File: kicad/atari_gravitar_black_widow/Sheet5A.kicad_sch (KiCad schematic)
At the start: 121 parts, among them Q2 2N6044, Q3 2N6044, Q4 2N6044

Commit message: more caps
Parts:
- C30, C33, C34: footprint Star_Wars_Vector_PCB:GenericComp -> Star_Wars_Vector_PCB:CapYellow
- C31, C32: footprint Star_Wars_Vector_PCB:SmallCap -> Star_Wars_Vector_PCB:CapBrown
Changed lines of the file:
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@@
       (effects (font (size 1.27 1.27)) (justify left))
     )
-    (property "Footprint" "Star_Wars_Vector_PCB:GenericComp" (id 2) (at 429.26 173.6598 0)
+    (property "Footprint" "Star_Wars_Vector_PCB:CapYellow" (id 2) (at 429.26 173.6598 0)
       (effects (font (size 1.27 1.27)) hide)
     )
@@
       (effects (font (size 1.27 1.27)) (justify left))
     )
-    (property "Footprint" "Star_Wars_Vector_PCB:GenericComp" (id 2) (at 445.135 111.4298 0)
+    (property "Footprint" "Star_Wars_Vector_PCB:CapYellow" (id 2) (at 445.135 111.4298 0)
       (effects (font (size 1.27 1.27)) hide)
     )
@@
       (effects (font (size 1.27 1.27)) (justify left))
     )
-    (property "Footprint" "Star_Wars_Vector_PCB:GenericComp" (id 2) (at 417.83 151.4348 0)
+    (property "Footprint" "Star_Wars_Vector_PCB:CapYellow" (id 2) (at 417.83 151.4348 0)
       (effects (font (size 1.27 1.27)) hide)
     )
@@
       (effects (font (size 1.27 1.27)) (justify left))
     )
-    (property "Footprint" "Star_Wars_Vector_PCB:SmallCap" (id 2) (at 385.7498 109.855 0)
+    (property "Footprint" "Star_Wars_Vector_PCB:CapBrown" (id 2) (at 385.7498 109.855 0)
       (effects (font (size 1.27 1.27)) hide)
     )
@@
       (effects (font (size 1.27 1.27)) (justify left))
     )
-    (property "Footprint" "Star_Wars_Vector_PCB:SmallCap" (id 2) (at 385.7498 172.085 0)
-      (effects (font (size 1.27 1.27)) hide)
-    )
+    (property "Footprint" "Star_Wars_Vector_PCB:CapBrown" (id 2) (at 385.7498 172.085 0)
+      (effects (font (size 1.27 1.27)) hide)
+    )

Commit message: more cap placements
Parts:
- C100, C101, C103, C104, C105, C106, C107, C108, C114, C115, C116, C90, C91, C92, C93, C94, C95, C96, C97, C98, C99: footprint (none) -> Star_Wars_Vector_PCB:GenericComp
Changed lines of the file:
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@@
       (effects (font (size 1.27 1.27)) (justify left))
     )
-    (property "Footprint" "" (id 2) (at 167.9702 234.95 0)
+    (property "Footprint" "Star_Wars_Vector_PCB:GenericComp" (id 2) (at 167.9702 234.95 0)
       (effects (font (size 1.27 1.27)) hide)
     )
@@
       (effects (font (size 1.27 1.27)) (justify left))
     )
-    (property "Footprint" "" (id 2) (at 133.6802 128.27 0)
+    (property "Footprint" "Star_Wars_Vector_PCB:GenericComp" (id 2) (at 133.6802 128.27 0)
       (effects (font (size 1.27 1.27)) hide)
     )
@@
       (effects (font (size 1.27 1.27)) (justify left))
     )
-    (property "Footprint" "" (id 2) (at 140.6652 128.27 0)
+    (property "Footprint" "Star_Wars_Vector_PCB:GenericComp" (id 2) (at 140.6652 128.27 0)
       (effects (font (size 1.27 1.27)) hide)
     )
@@
       (effects (font (size 1.27 1.27)) (justify left))
     )
-    (property "Footprint" "" (id 2) (at 126.6952 304.8 0)
+    (property "Footprint" "Star_Wars_Vector_PCB:GenericComp" (id 2) (at 126.6952 304.8 0)
       (effects (font (size 1.27 1.27)) hide)
     )
@@
       (effects (font (size 1.27 1.27)) (justify left))
     )
-    (property "Footprint" "" (id 2) (at 119.7102 304.8 0)
+    (property "Footprint" "Star_Wars_Vector_PCB:GenericComp" (id 2) (at 119.7102 304.8 0)
       (effects (font (size 1.27 1.27)) hide)
     )
@@
       (effects (font (size 1.27 1.27)) (justify left))
     )
-    (property "Footprint" "" (id 2) (at 154.6352 234.95 0)
+    (property "Footprint" "Star_Wars_Vector_PCB:GenericComp" (id 2) (at 154.6352 234.95 0)
       (effects (font (size 1.27 1.27)) hide)
     )
@@
       (effects (font (size 1.27 1.27)) (justify left))
     )
-    (property "Footprint" "" (id 2) (at 119.7102 128.27 0)
+    (property "Footprint" "Star_Wars_Vector_PCB:GenericComp" (id 2) (at 119.7102 128.27 0)
       (effects (font (size 1.27 1.27)) hide)
     )
@@
       (effects (font (size 1.27 1.27)) (justify left))
     )
-    (property "Footprint" "" (id 2) (at 160.9852 128.27 0)
+    (property "Footprint" "Star_Wars_Vector_PCB:GenericComp" (id 2) (at 160.9852 128.27 0)
       (effects (font (size 1.27 1.27)) hide)
     )
@@
       (effects (font (size 1.27 1.27)) (justify left))
     )
-    (property "Footprint" "" (id 2) (at 112.7252 304.8 0)
+    (property "Footprint" "Star_Wars_Vector_PCB:GenericComp" (id 2) (at 112.7252 304.8 0)
       (effects (font (size 1.27 1.27)) hide)
     )
@@
       (effects (font (size 1.27 1.27)) (justify left))
     )
-    (property "Footprint" "" (id 2) (at 154.0002 128.27 0)
+    (property "Footprint" "Star_Wars_Vector_PCB:GenericComp" (id 2) (at 154.0002 128.27 0)
       (effects (font (size 1.27 1.27)) hide)
     )
@@
       (effects (font (size 1.27 1.27)) (justify left))
     )
-    (property "Footprint" "" (id 2) (at 378.1552 294.64 0)
+    (property "Footprint" "Star_Wars_Vector_PCB:GenericComp" (id 2) (at 378.1552 294.64 0)
       (effects (font (size 1.27 1.27)) hide)
     )
@@
       (effects (font (size 1.27 1.27)) (justify left))
     )
-    (property "Footprint" "" (id 2) (at 140.6652 234.95 0)
+    (property "Footprint" "Star_Wars_Vector_PCB:GenericComp" (id 2) (at 140.6652 234.95 0)
       (effects (font (size 1.27 1.27)) hide)
     )
@@
       (effects (font (size 1.27 1.27)) (justify left))
     )
-    (property "Footprint" "" (id 2) (at 126.6952 128.27 0)
+    (property "Footprint" "Star_Wars_Vector_PCB:GenericComp" (id 2) (at 126.6952 128.27 0)
       (effects (font (size 1.27 1.27)) hide)
     )
@@
       (effects (font (size 1.27 1.27)) (justify left))
     )
-    (property "Footprint" "" (id 2) (at 167.9702 128.27 0)
+    (property "Footprint" "Star_Wars_Vector_PCB:GenericComp" (id 2) (at 167.9702 128.27 0)
       (effects (font (size 1.27 1.27)) hide)
     )
@@
       (effects (font (size 1.27 1.27)) (justify left))
     )
-    (property "Footprint" "" (id 2) (at 147.0152 128.27 0)
+    (property "Footprint" "Star_Wars_Vector_PCB:GenericComp" (id 2) (at 147.0152 128.27 0)
       (effects (font (size 1.27 1.27)) hide)
     )
@@
       (effects (font (size 1.27 1.27)) (justify left))
     )
-    (property "Footprint" "" (id 2) (at 147.6502 234.95 0)
+    (property "Footprint" "Star_Wars_Vector_PCB:GenericComp" (id 2) (at 147.6502 234.95 0)
       (effects (font (size 1.27 1.27)) hide)
     )
@@
       (effects (font (size 1.27 1.27)) (justify left))
     )
-    (property "Footprint" "" (id 2) (at 378.1552 271.78 0)
+    (property "Footprint" "Star_Wars_Vector_PCB:GenericComp" (id 2) (at 378.1552 271.78 0)
       (effects (font (size 1.27 1.27)) hide)
     )
@@
       (effects (font (size 1.27 1.27)) (justify left))
     )
-    (property "Footprint" "" (id 2) (at 378.1552 313.055 0)
+    (property "Footprint" "Star_Wars_Vector_PCB:GenericComp" (id 2) (at 378.1552 313.055 0)
       (effects (font (size 1.27 1.27)) hide)
     )
@@
       (effects (font (size 1.27 1.27)) (justify left))
     )
-    (property "Footprint" "" (id 2) (at 161.6202 234.95 0)
+    (property "Footprint" "Star_Wars_Vector_PCB:GenericComp" (id 2) (at 161.6202 234.95 0)
       (effects (font (size 1.27 1.27)) hide)
     )
@@
       (effects (font (size 1.27 1.27)) (justify left))
     )
-    (property "Footprint" "" (id 2) (at 105.7402 304.8 0)
+    (property "Footprint" "Star_Wars_Vector_PCB:GenericComp" (id 2) (at 105.7402 304.8 0)
       (effects (font (size 1.27 1.27)) hide)
     )
@@
       (effects (font (size 1.27 1.27)) (justify left))
     )
-    (property "Footprint" "" (id 2) (at 133.0452 304.8 0)
-      (effects (font (size 1.27 1.27)) hide)
-    )
+    (property "Footprint" "Star_Wars_Vector_PCB:GenericComp" (id 2) (at 133.0452 304.8 0)
+      (effects (font (size 1.27 1.27)) hide)
+    )

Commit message: more cap placements
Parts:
- C31, C32: footprint Star_Wars_Vector_PCB:CapBrown -> quantum_arcade_pcb:CapSmall
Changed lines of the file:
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@@
       (effects (font (size 1.27 1.27)) (justify left))
     )
-    (property "Footprint" "Star_Wars_Vector_PCB:CapBrown" (id 2) (at 385.7498 109.855 0)
+    (property "Footprint" "quantum_arcade_pcb:CapSmall" (id 2) (at 385.7498 109.855 0)
       (effects (font (size 1.27 1.27)) hide)
     )
@@
       (effects (font (size 1.27 1.27)) (justify left))
     )
-    (property "Footprint" "Star_Wars_Vector_PCB:CapBrown" (id 2) (at 385.7498 172.085 0)
+    (property "Footprint" "quantum_arcade_pcb:CapSmall" (id 2) (at 385.7498 172.085 0)
       (effects (font (size 1.27 1.27)) hide)
     )

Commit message: resistor placements R1-R153
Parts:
- C30: footprint Star_Wars_Vector_PCB:CapYellow -> Star_Wars_Vector_PCB:CapElec2
- R102, R103, R104, R105, R106, R108, R109, R110, R111, R112, R113, R114, R115, R116, R117, R118, R119, R121, R122, R123, R124, R125, R126, R127, R128, R129, R130, R131, R133, R134, R135, R136, R137, R138, R139, R140, R141, R142, R143, R144, R145, R146, R147, R148, R24, R25, R26, R27, R28, R29, R30, R31, R32, R33, R34, R35, R36, R37, R38, R39, R43, R44, R45, R46, R47, R48, R49, R50, R51, R52, R53, R54: footprint (none) -> Star_Wars_Vector_PCB:GenericComp

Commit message: caps
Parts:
- C30: footprint Star_Wars_Vector_PCB:CapElec2 -> Star_Wars_Vector_PCB:Inductor1
- C33: footprint Star_Wars_Vector_PCB:CapYellow -> Star_Wars_Vector_PCB:Inductor1
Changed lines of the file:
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@@
       (effects (font (size 1.27 1.27)) (justify left))
     )
-    (property "Footprint" "Star_Wars_Vector_PCB:CapYellow" (id 2) (at 429.26 173.6598 0)
+    (property "Footprint" "Star_Wars_Vector_PCB:Inductor1" (id 2) (at 429.26 173.6598 0)
       (effects (font (size 1.27 1.27)) hide)
     )
@@
       (effects (font (size 1.27 1.27)) (justify left))
     )
-    (property "Footprint" "Star_Wars_Vector_PCB:CapElec2" (id 2) (at 445.135 111.4298 0)
+    (property "Footprint" "Star_Wars_Vector_PCB:Inductor1" (id 2) (at 445.135 111.4298 0)
       (effects (font (size 1.27 1.27)) hide)
     )

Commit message: ALL PARTS PLACED!!
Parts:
- B_4, D_4: footprint (none) -> Star_Wars_Vector_PCB:DIP16
- P_10: footprint (none) -> Star_Wars_Vector_PCB:DIP8
- Q2, Q3, Q4: footprint (none) -> quantum_arcade_pcb:BigTrans
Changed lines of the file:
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@@
     (property "Reference" "B_4" (id 0) (at 287.02 89.9668 0))
     (property "Value" "8 DIP SW" (id 1) (at 287.02 87.6554 0))
-    (property "Footprint" "" (id 2) (at 287.02 75.565 0)
+    (property "Footprint" "Star_Wars_Vector_PCB:DIP16" (id 2) (at 287.02 75.565 0)
       (effects (font (size 1.27 1.27)) hide)
     )
@@
       (effects (font (size 1.27 1.27)) (justify left))
     )
-    (property "Footprint" "" (id 2) (at 361.95 306.705 0)
+    (property "Footprint" "quantum_arcade_pcb:BigTrans" (id 2) (at 361.95 306.705 0)
       (effects (font (size 1.27 1.27)) hide)
     )
@@
     (property "Reference" "P_10" (id 0) (at 395.605 316.0735 0))
     (property "Value" "SW4POS" (id 1) (at 395.605 318.8486 0))
-    (property "Footprint" "" (id 2) (at 395.605 325.12 0)
+    (property "Footprint" "Star_Wars_Vector_PCB:DIP8" (id 2) (at 395.605 325.12 0)
       (effects (font (size 1.27 1.27)) hide)
     )
@@
       (effects (font (size 1.27 1.27)) (justify left))
     )
-    (property "Footprint" "" (id 2) (at 361.95 265.43 0)
+    (property "Footprint" "quantum_arcade_pcb:BigTrans" (id 2) (at 361.95 265.43 0)
       (effects (font (size 1.27 1.27)) hide)
     )
@@
     (property "Reference" "D_4" (id 0) (at 287.02 152.1968 0))
     (property "Value" "8 DIP SW" (id 1) (at 287.02 149.8854 0))
-    (property "Footprint" "" (id 2) (at 287.02 137.795 0)
+    (property "Footprint" "Star_Wars_Vector_PCB:DIP16" (id 2) (at 287.02 137.795 0)
       (effects (font (size 1.27 1.27)) hide)
     )
@@
       (effects (font (size 1.27 1.27)) (justify left))
     )
-    (property "Footprint" "" (id 2) (at 361.95 288.29 0)
+    (property "Footprint" "quantum_arcade_pcb:BigTrans" (id 2) (at 361.95 288.29 0)
       (effects (font (size 1.27 1.27)) hide)
     )
@@
     (property "Reference" "P_10" (id 0) (at 86.36 181.4535 0))
     (property "Value" "SW4POS" (id 1) (at 86.36 184.2286 0))
-    (property "Footprint" "" (id 2) (at 86.36 190.5 0)
-      (effects (font (size 1.27 1.27)) hide)
-    )
+    (property "Footprint" "Star_Wars_Vector_PCB:DIP8" (id 2) (at 86.36 190.5 0)
+      (effects (font (size 1.27 1.27)) hide)
+    )

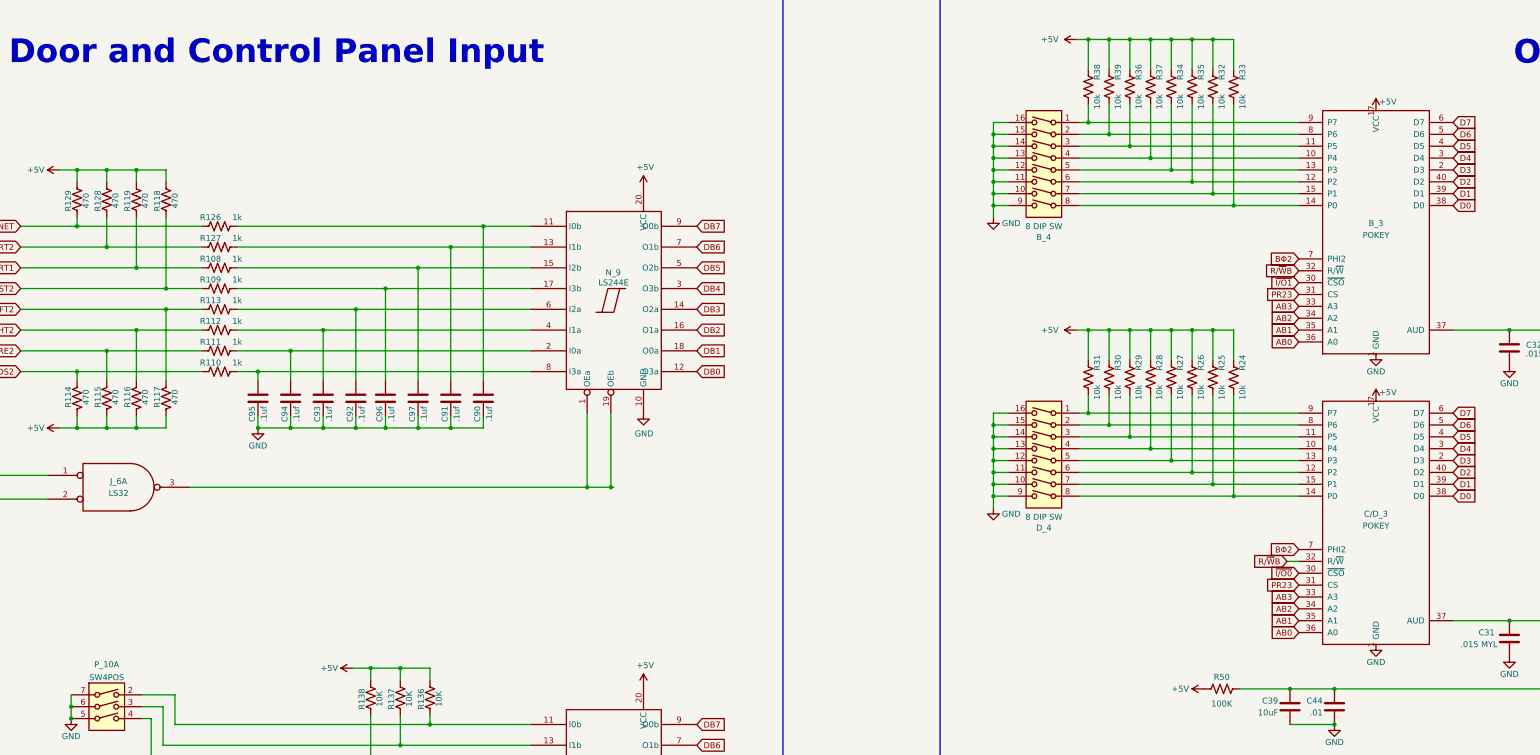
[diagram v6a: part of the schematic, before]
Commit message: Fixed all schematic warnings and fixed the edge cuts
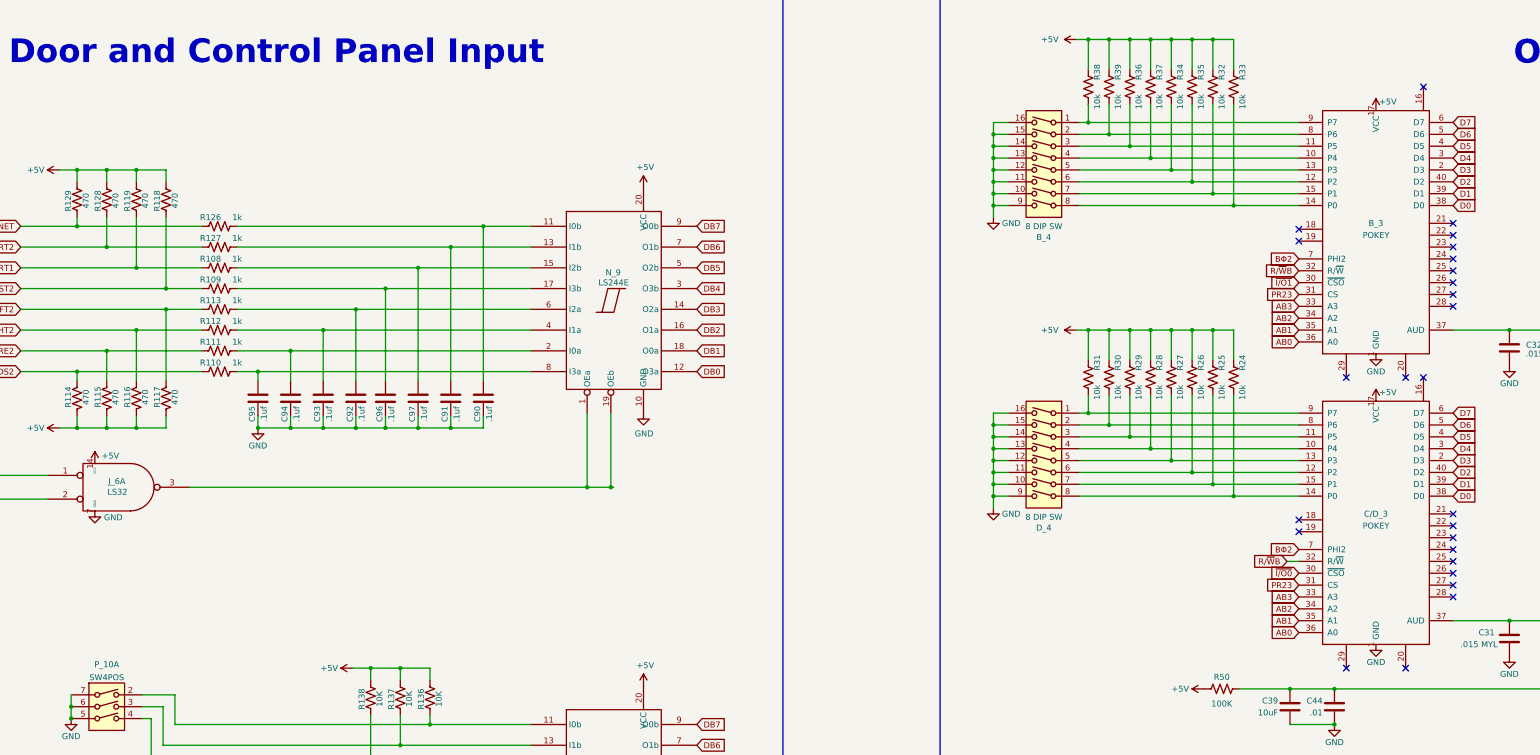
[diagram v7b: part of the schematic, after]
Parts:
- removed J_6: LS32, Star_Wars_Vector_PCB:DIP14, symbol atari_grav_bw:LS32
- added J_6: LS32, Star_Wars_Vector_PCB:DIP14, symbol Star_Wars_Vector_PCB:LS32
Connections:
- no-connect marks 0 -> 26
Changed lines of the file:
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@@
   (junction (at 132.715 109.855) (diameter 0) (color 0 0 0 0)
   )
+  (no_connect (at 341.63 88.265))
+  (no_connect (at 341.63 90.805))
+  (no_connect (at 374.65 92.075))
+  (no_connect (at 374.65 94.615))
+  (no_connect (at 374.65 97.155))
+  (no_connect (at 374.65 99.695))
+  (no_connect (at 374.65 86.995))
+  (no_connect (at 374.65 89.535))
+  (no_connect (at 374.65 102.235))
+  (no_connect (at 374.65 104.775))
+  (no_connect (at 351.79 120.015))
+  (no_connect (at 368.3 57.785))
+  (no_connect (at 364.49 182.245))
+  (no_connect (at 351.79 182.245))
+  (no_connect (at 374.65 156.845))
+  (no_connect (at 374.65 159.385))
+  (no_connect (at 374.65 161.925))
+  (no_connect (at 374.65 164.465))
+  (no_connect (at 374.65 167.005))
+  (no_connect (at 341.63 153.035))
+  (no_connect (at 341.63 150.495))
+  (no_connect (at 368.3 120.015))
+  (no_connect (at 374.65 149.225))
+  (no_connect (at 374.65 151.765))
+  (no_connect (at 374.65 154.305))
+  (no_connect (at 364.49 120.015))
   (wire (pts (xy 499.745 101.6) (xy 499.745 92.71))
     (stroke (width 0) (type default) (color 0 0 0 0))
@@
     (pin "2")
   )
+  (symbol (lib_id "power:GND") (at 83.82 148.59 0) (unit 1)
+    (in_bom yes) (on_board yes)
+    (property "Reference" "#PWR0543" (id 0) (at 83.82 154.94 0)
+      (effects (font (size 1.27 1.27)) hide)
+    )
+    (property "Value" "GND" (id 1) (at 87.757 149.987 0))
+    (property "Footprint" "" (id 2) (at 83.82 148.59 0)
+      (effects (font (size 1.27 1.27)) hide)
+    )
+    (property "Datasheet" "" (id 3) (at 83.82 148.59 0)
+      (effects (font (size 1.27 1.27)) hide)
+    )
+    (pin "1")
+  )
   (symbol (lib_id "power:+5V") (at 358.14 125.095 0) (unit 1)
     (in_bom yes) (on_board yes)
@@
     (pin "1")
   )
+  (symbol (lib_id "power:+5V") (at 83.82 138.43 0) (mirror y) (unit 1)
+    (in_bom yes) (on_board yes)
+    (property "Reference" "#PWR0544" (id 0) (at 83.82 142.24 0)
+      (effects (font (size 1.27 1.27)) hide)
+    )
+    (property "Value" "+5V" (id 1) (at 89.027 136.779 0)
+      (effects (font (size 1.27 1.27)) (justify left))
+    )
+    (property "Footprint" "" (id 2) (at 83.82 138.43 0)
+      (effects (font (size 1.27 1.27)) hide)
+    )
+    (property "Datasheet" "" (id 3) (at 83.82 138.43 0)
+      (effects (font (size 1.27 1.27)) hide)
+    )
+    (pin "1")
+  )
   (symbol (lib_id "Device:R_US") (at 300.99 57.785 180) (unit 1)
     (in_bom yes) (on_board yes)
@@
     (pin "14")
     (pin "15")
+    (pin "16")
     (pin "17")
+    (pin "18")
+    (pin "19")
     (pin "2")
+    (pin "20")
+    (pin "21")
+    (pin "22")
+    (pin "23")
+    (pin "24")
+    (pin "25")
+    (pin "26")
+    (pin "27")
+    (pin "28")
+    (pin "29")
     (pin "3")
     (pin "30")
@@
     (pin "2")
   )
-  (symbol (lib_id "atari_grav_bw:LS32") (at 88.9 143.51 0) (unit 1) (convert 2)
-    (in_bom yes) (on_board yes)
-    (property "Reference" "J_6" (id 0) (at 88.9 142.24 0))
-    (property "Value" "LS32" (id 1) (at 88.9 144.78 0))
-    (property "Footprint" "Star_Wars_Vector_PCB:DIP14" (id 2) (at 88.9 143.51 0)
-      (effects (font (size 1.27 1.27)) hide)
-    )
-    (property "Datasheet" "" (id 3) (at 88.9 143.51 0)
-      (effects (font (size 1.27 1.27)) hide)
-    )
-    (pin "1")
-    (pin "2")
-    (pin "3")
-  )
   (symbol (lib_id "Amplifier_Operational:LM324A") (at 514.35 180.34 0) (mirror x) (unit 1)
     (in_bom yes) (on_board yes)
@@
     (pin "2")
   )
+  (symbol (lib_id "Star_Wars_Vector_PCB:LS32") (at 88.9 143.51 0) (unit 1) (convert 2)
+    (in_bom yes) (on_board yes)
+    (property "Reference" "J_6" (id 0) (at 88.519 142.24 0))
+    (property "Value" "LS32" (id 1) (at 88.646 144.526 0))
+    (property "Footprint" "Star_Wars_Vector_PCB:DIP14" (id 2) (at 88.9 143.51 0)
+      (effects (font (size 1.27 1.27)) hide)
+    )
+    (property "Datasheet" "" (id 3) (at 88.9 143.51 0)
+      (effects (font (size 1.27 1.27)) hide)
+    )
+    (pin "1")
+    (pin "14")
+    (pin "2")
+    (pin "3")
+    (pin "7")
+  )
   (symbol (lib_id "quantum_arcade_pcb:POKEY") (at 358.14 150.495 0) (unit 1)
     (in_bom yes) (on_board yes)
@@
     (pin "14")
     (pin "15")
+    (pin "16")
     (pin "17")
+    (pin "18")
+    (pin "19")
     (pin "2")
+    (pin "20")
+    (pin "21")
+    (pin "22")
+    (pin "23")
+    (pin "24")
+    (pin "25")
+    (pin "26")
+    (pin "27")
+    (pin "28")
+    (pin "29")
     (pin "3")
     (pin "30")
